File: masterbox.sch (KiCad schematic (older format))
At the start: 0 parts

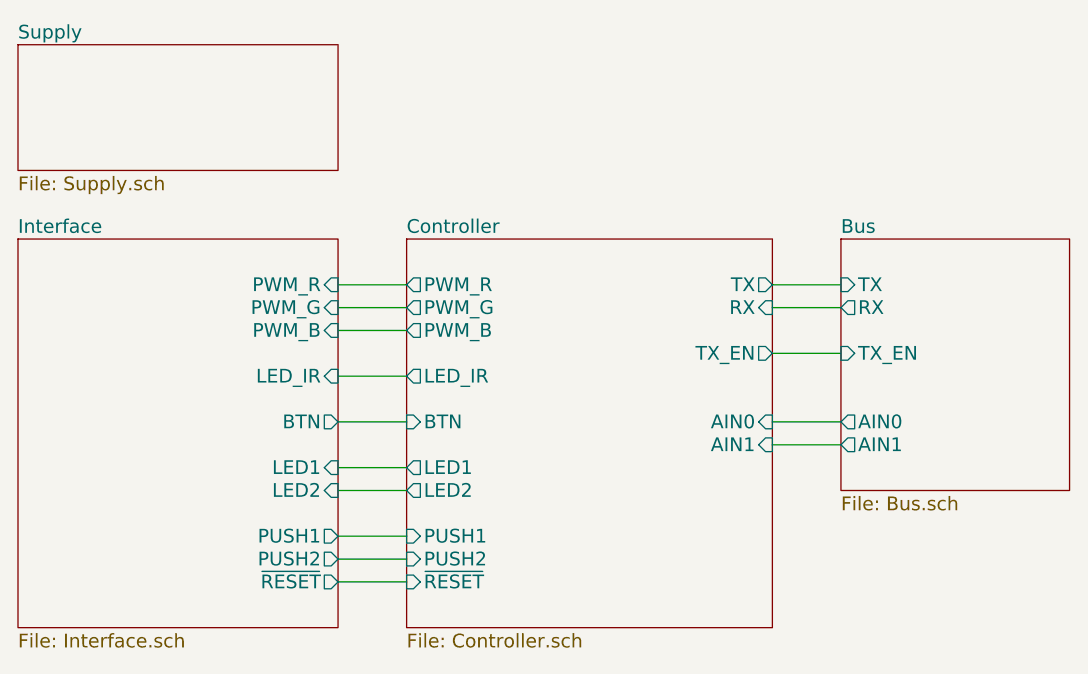
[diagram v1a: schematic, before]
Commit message: ATmega2560 inserted
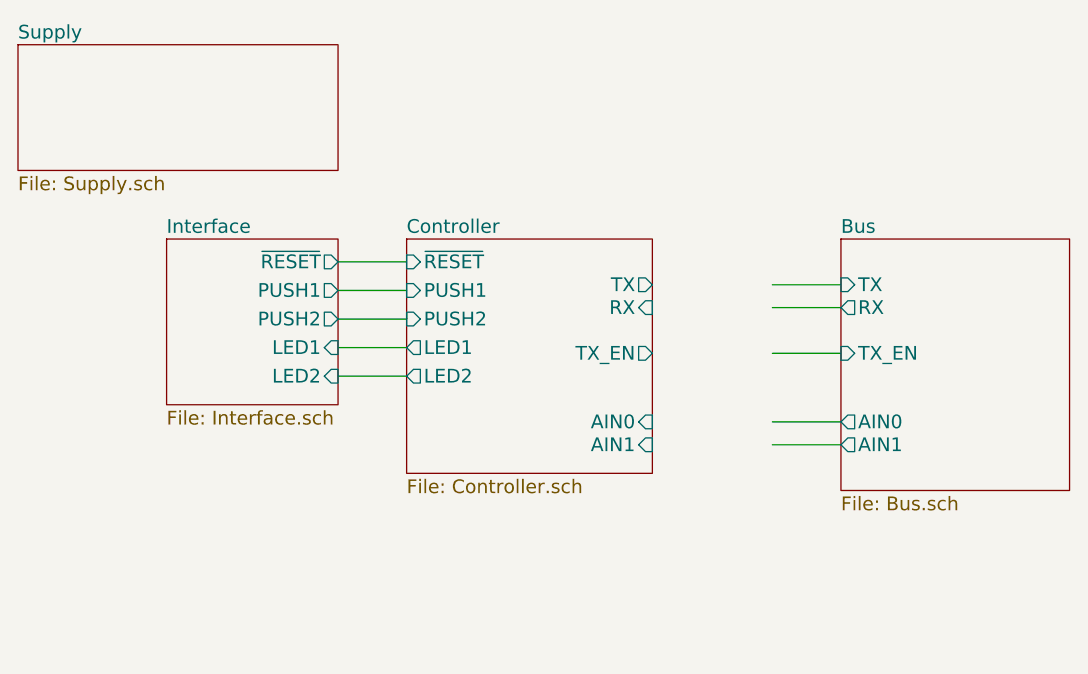
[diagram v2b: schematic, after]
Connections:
- wire segments 15 -> 11
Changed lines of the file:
@@
 $EndSheet
 $Sheet
-S 3300 3600 1400 1700
+S 3950 3600 750  725
 U 59DBA5DF
 F0 "Interface" 60
 F1 "Interface.sch" 60
-F2 "LED_IR" I R 4700 4200 60
-F3 "PWM_R" I R 4700 3800 60
-F4 "PWM_G" I R 4700 3900 60
-F5 "PWM_B" I R 4700 4000 60
-F6 "BTN" O R 4700 4400 60
-F7 "~RESET" O R 4700 5100 60
-F8 "PUSH1" O R 4700 4900 60
-F9 "PUSH2" O R 4700 5000 60
-F10 "LED1" I R 4700 4600 60
-F11 "LED2" I R 4700 4700 60
+F2 "~RESET" O R 4700 3700 60
+F3 "PUSH1" O R 4700 3825 60
+F4 "PUSH2" O R 4700 3950 60
+F5 "LED1" I R 4700 4075 60
+F6 "LED2" I R 4700 4200 60
 $EndSheet
 $Sheet
-S 5000 3600 1600 1700
+S 5000 3600 1075 1025
 U 59DB9B58
 F0 "Controller" 60
 F1 "Controller.sch" 60
-F2 "PWM_R" O L 5000 3800 60
-F3 "PWM_G" O L 5000 3900 60
-F4 "TX_EN" O R 6600 4100 60
-F5 "RX" I R 6600 3900 60
-F6 "TX" O R 6600 3800 60
-F7 "PWM_B" O L 5000 4000 60
-F8 "BTN" I L 5000 4400 60
-F9 "LED_IR" O L 5000 4200 60
-F10 "AIN0" I R 6600 4400 60
-F11 "AIN1" I R 6600 4500 60
-F12 "LED1" O L 5000 4600 60
-F13 "LED2" O L 5000 4700 60
-F14 "PUSH1" I L 5000 4900 60
-F15 "PUSH2" I L 5000 5000 60
-F16 "~RESET" I L 5000 5100 60
+F2 "TX_EN" O R 6075 4100 60
+F3 "RX" I R 6075 3900 60
+F4 "TX" O R 6075 3800 60
+F5 "AIN0" I R 6075 4400 60
+F6 "AIN1" I R 6075 4500 60
+F7 "LED1" O L 5000 4075 60
+F8 "LED2" O L 5000 4200 60
+F9 "PUSH1" I L 5000 3825 60
+F10 "PUSH2" I L 5000 3950 60
+F11 "~RESET" I L 5000 3700 60
 $EndSheet
 $Sheet
@@
 	6600 4500 6900 4500
 Wire Wire Line
-	5000 3800 4700 3800
+	4700 3700 5000 3700
 Wire Wire Line
-	4700 3900 5000 3900
+	5000 3825 4700 3825
 Wire Wire Line
-	5000 4000 4700 4000
+	4700 3950 5000 3950
 Wire Wire Line
-	5000 4200 4700 4200
+	5000 3950 5000 3925
 Wire Wire Line
-	4700 4400 5000 4400
+	5000 4075 4700 4075
 Wire Wire Line
-	5000 4600 4700 4600
-Wire Wire Line
-	4700 4700 5000 4700
-Wire Wire Line
-	5000 4900 4700 4900
-Wire Wire Line
-	4700 5000 5000 5000
-Wire Wire Line
-	5000 5100 4700 5100
+	4700 4200 5000 4200
 $EndSCHEMATC
